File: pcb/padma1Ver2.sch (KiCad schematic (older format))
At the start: 15 parts, among them SW1 SPST, U1 NodeMCU_Amica_R2

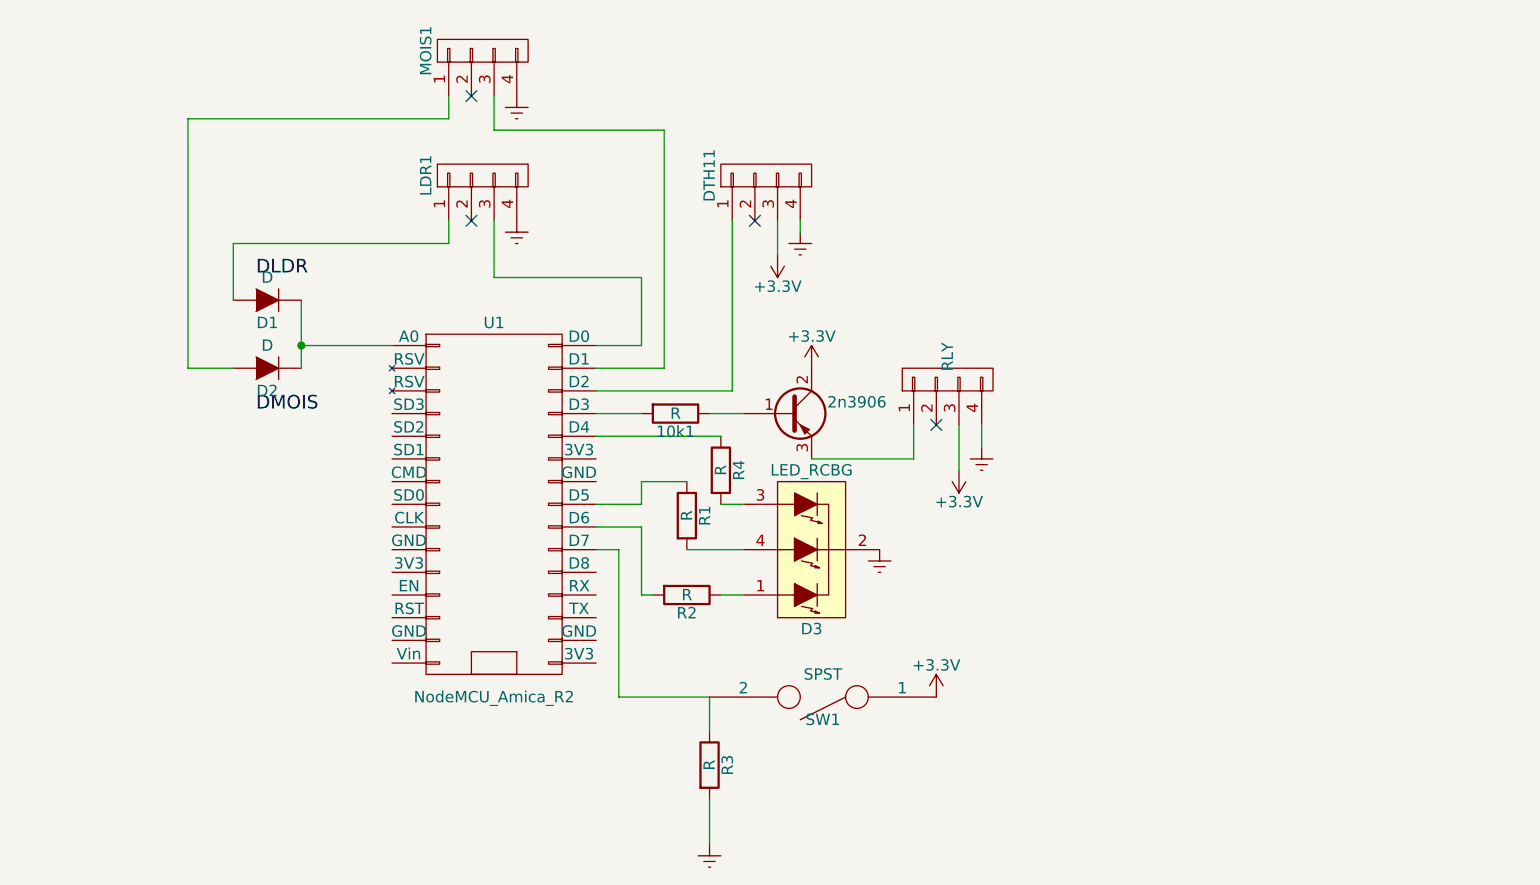
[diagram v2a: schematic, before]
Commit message: with no electrical errors
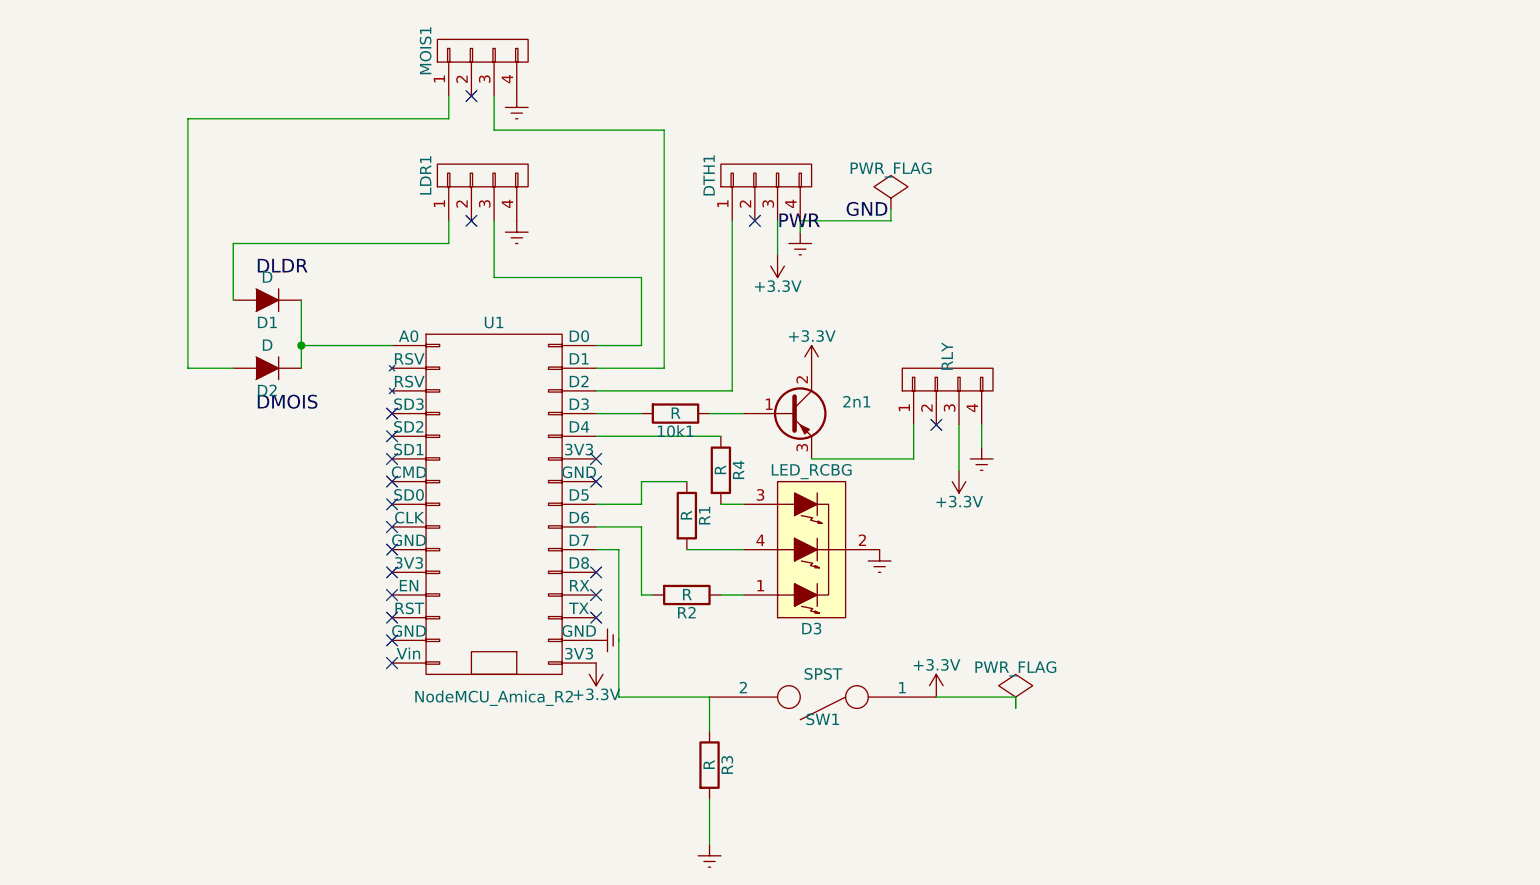
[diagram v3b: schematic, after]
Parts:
- renumbered 2n3906 to 2n1, DTH11 to DTH1
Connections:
- net +3V3: now also U1.16 (3V3)
- net Earth: now also U1.17 (GND)
- no-connect marks 4 -> 21
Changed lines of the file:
@@
 $EndDescr
-$Comp
-L NodeMCU_Amica_R2 U1
-U 1 1 582C3605
-P 4650 3500
-F 0 "U1" H 4650 4300 50  0000 C CNN
-F 1 "NodeMCU_Amica_R2" H 4650 2650 50  0000 C CNN
-F 2 "" H 4900 3500 50  0000 C CNN
-F 3 "" H 4900 3500 50  0000 C CNN
-	1    4650 3500
-	1    0    0    -1
-$EndComp
 $Comp
 L R R3
@@
 $EndComp
 $Comp
-L Q_PNP_BCE 2n3906
+L Q_PNP_BCE 2n1
 U 1 1 582C37C4
 P 5950 3100
-F 0 "2n3906" H 6250 3150 50  0000 C CNN
+F 0 "2n1" H 6250 3150 50  0000 C CNN
 F 1 "Q_PNP_BCE" H 6550 3050 50  0001 R CNN
 F 2 "" H 6150 3200 50  0000 C CNN
@@
 $EndComp
 $Comp
-L CONN_01X04 DTH11
+L CONN_01X04 DTH1
 U 1 1 582C4013
 P 5850 2050
-F 0 "DTH11" H 5850 2300 50  0000 C CNN
+F 0 "DTH1" H 5850 2300 50  0000 C CNN
 F 1 "CONN_01X04" V 5950 2050 50  0001 C CNN
 F 2 "" H 5850 2050 50  0000 C CNN
@@
 NoConn ~ 4550 1700
 $Comp
-L Earth #PWR2
+L Earth #PWR01
 U 1 1 582C4AC2
 P 4750 2250
-F 0 "#PWR2" H 4750 2000 50  0001 C CNN
+F 0 "#PWR01" H 4750 2000 50  0001 C CNN
 F 1 "Earth" H 4750 2100 50  0001 C CNN
 F 2 "" H 4750 2250 50  0000 C CNN
@@
 $EndComp
 $Comp
-L +3.3V #PWR6
+L +3.3V #PWR02
 U 1 1 582C5C13
 P 6050 2900
-F 0 "#PWR6" H 6050 2750 50  0001 C CNN
+F 0 "#PWR02" H 6050 2750 50  0001 C CNN
 F 1 "+3.3V" H 6050 3040 50  0000 C CNN
 F 2 "" H 6050 2900 50  0000 C CNN
@@
 $EndComp
 $Comp
-L Earth #PWR1
+L Earth #PWR03
 U 1 1 582C693C
 P 4750 1700
-F 0 "#PWR1" H 4750 1450 50  0001 C CNN
+F 0 "#PWR03" H 4750 1450 50  0001 C CNN
 F 1 "Earth" H 4750 1550 50  0001 C CNN
 F 2 "" H 4750 1700 50  0000 C CNN
@@
 NoConn ~ 5800 2250
 $Comp
-L +3.3V #PWR4
+L +3.3V #PWR04
 U 1 1 582C7499
 P 5900 2400
-F 0 "#PWR4" H 5900 2250 50  0001 C CNN
+F 0 "#PWR04" H 5900 2250 50  0001 C CNN
 F 1 "+3.3V" H 5900 2540 50  0000 C CNN
 F 2 "" H 5900 2400 50  0000 C CNN
@@
 $EndComp
 $Comp
-L Earth #PWR5
+L Earth #PWR05
 U 1 1 582C7550
 P 6000 2300
-F 0 "#PWR5" H 6000 2050 50  0001 C CNN
+F 0 "#PWR05" H 6000 2050 50  0001 C CNN
 F 1 "Earth" H 6000 2150 50  0001 C CNN
 F 2 "" H 6000 2300 50  0000 C CNN
@@
 NoConn ~ 6600 3150
 $Comp
-L +3.3V #PWR9
+L +3.3V #PWR06
 U 1 1 582C78ED
 P 6700 3350
-F 0 "#PWR9" H 6700 3200 50  0001 C CNN
+F 0 "#PWR06" H 6700 3200 50  0001 C CNN
 F 1 "+3.3V" H 6700 3490 50  0000 C CNN
 F 2 "" H 6700 3350 50  0000 C CNN
@@
 $EndComp
 $Comp
-L Earth #PWR10
+L Earth #PWR07
 U 1 1 582C79CF
 P 6800 3250
-F 0 "#PWR10" H 6800 3000 50  0001 C CNN
+F 0 "#PWR07" H 6800 3000 50  0001 C CNN
 F 1 "Earth" H 6800 3100 50  0001 C CNN
 F 2 "" H 6800 3250 50  0000 C CNN
@@
 $EndComp
 $Comp
-L Earth #PWR7
+L Earth #PWR08
 U 1 1 582C8C6A
 P 6350 3700
-F 0 "#PWR7" H 6350 3450 50  0001 C CNN
+F 0 "#PWR08" H 6350 3450 50  0001 C CNN
 F 1 "Earth" H 6350 3550 50  0001 C CNN
 F 2 "" H 6350 3700 50  0000 C CNN
@@
 	1    0    0    -1
 $EndComp
-Wire Wire Line
-	3800 2600 3800 2900
-Wire Wire Line
-	4200 2800 3800 2800
-Connection ~ 3800 2800
-Wire Wire Line
-	3500 2600 3500 2350
-Wire Wire Line
-	3300 2900 3500 2900
-Wire Wire Line
-	3300 1800 3300 2900
-Wire Wire Line
-	3300 1800 4450 1800
-Wire Wire Line
-	4450 1800 4450 1700
-Wire Wire Line
-	3500 2350 4450 2350
-Wire Wire Line
-	4450 2350 4450 2250
-Wire Wire Line
-	5100 2800 5300 2800
-Wire Wire Line
-	5300 2800 5300 2500
-Wire Wire Line
-	5300 2500 4650 2500
-Wire Wire Line
-	4650 2500 4650 2250
-Wire Wire Line
-	5100 2900 5400 2900
-Wire Wire Line
-	5100 3100 5300 3100
-Wire Wire Line
-	5600 3100 5750 3100
-Wire Wire Line
-	4650 1700 4650 1850
-Wire Wire Line
-	4650 1850 5400 1850
-Wire Wire Line
-	5400 1850 5400 2900
-Wire Wire Line
-	5100 3000 5700 3000
-Wire Wire Line
-	5700 3000 5700 2250
-Wire Wire Line
-	5900 2250 5900 2400
-Wire Wire Line
-	6000 2250 6000 2300
-Wire Wire Line
-	6050 3300 6500 3300
-Wire Wire Line
-	6500 3300 6500 3150
-Wire Wire Line
-	6700 3350 6700 3150
-Wire Wire Line
-	6800 3250 6800 3150
-Wire Wire Line
-	5100 3200 5650 3200
-Wire Wire Line
-	5650 3500 5750 3500
-Wire Wire Line
-	5100 3500 5300 3500
-Wire Wire Line
-	5300 3500 5300 3400
-Wire Wire Line
-	5300 3400 5500 3400
-Wire Wire Line
-	5500 3700 5750 3700
-Wire Wire Line
-	5650 3900 5750 3900
-Wire Wire Line
-	5100 3600 5300 3600
-Wire Wire Line
-	5300 3600 5300 3900
-Wire Wire Line
-	5300 3900 5350 3900
-Wire Wire Line
-	5600 4500 5600 4350
-Wire Wire Line
-	5100 3700 5200 3700
-Wire Wire Line
-	5200 3700 5200 4350
-Wire Wire Line
-	5200 4350 5600 4350
-$Comp
-L Earth #PWR3
+$Comp
+L Earth #PWR09
 U 1 1 582C92CF
 P 5600 5000
-F 0 "#PWR3" H 5600 4750 50  0001 C CNN
+F 0 "#PWR09" H 5600 4750 50  0001 C CNN
 F 1 "Earth" H 5600 4850 50  0001 C CNN
 F 2 "" H 5600 5000 50  0000 C CNN
@@
 	1    0    0    -1
 $EndComp
-Wire Wire Line
-	5600 5000 5600 4800
-$Comp
-L +3.3V #PWR8
+$Comp
+L +3.3V #PWR010
 U 1 1 582C937E
 P 6600 4350
-F 0 "#PWR8" H 6600 4200 50  0001 C CNN
+F 0 "#PWR010" H 6600 4200 50  0001 C CNN
 F 1 "+3.3V" H 6600 4490 50  0000 C CNN
 F 2 "" H 6600 4350 50  0000 C CNN
@@
 	1    0    0    -1
 $EndComp
+$Comp
+L PWR_FLAG #FLG011
+U 1 1 582CAB1D
+P 6400 2200
+F 0 "#FLG011" H 6400 2295 50  0001 C CNN
+F 1 "PWR_FLAG" H 6400 2380 50  0000 C CNN
+F 2 "" H 6400 2200 50  0000 C CNN
+F 3 "" H 6400 2200 50  0000 C CNN
+	1    6400 2200
+	1    0    0    -1
+$EndComp
+$Comp
+L PWR_FLAG #FLG012
+U 1 1 582CAB85
+P 6950 4400
+F 0 "#FLG012" H 6950 4495 50  0001 C CNN
+F 1 "PWR_FLAG" H 6950 4580 50  0000 C CNN
+F 2 "" H 6950 4400 50  0000 C CNN
+F 3 "" H 6950 4400 50  0000 C CNN
+	1    6950 4400
+	1    0    0    -1
+$EndComp
+Wire Wire Line
+	3800 2600 3800 2900
+Wire Wire Line
+	4200 2800 3800 2800
+Connection ~ 3800 2800
+Wire Wire Line
+	3500 2600 3500 2350
+Wire Wire Line
+	3300 2900 3500 2900
+Wire Wire Line
+	3300 1800 3300 2900
+Wire Wire Line
+	3300 1800 4450 1800
+Wire Wire Line
+	4450 1800 4450 1700
+Wire Wire Line
+	3500 2350 4450 2350
+Wire Wire Line
+	4450 2350 4450 2250
+Wire Wire Line
+	5100 2800 5300 2800
+Wire Wire Line
+	5300 2800 5300 2500
+Wire Wire Line
+	5300 2500 4650 2500
+Wire Wire Line
+	4650 2500 4650 2250
+Wire Wire Line
+	5100 2900 5400 2900
+Wire Wire Line
+	5100 3100 5300 3100
+Wire Wire Line
+	5600 3100 5750 3100
+Wire Wire Line
+	4650 1700 4650 1850
+Wire Wire Line
+	4650 1850 5400 1850
+Wire Wire Line
+	5400 1850 5400 2900
+Wire Wire Line
+	5100 3000 5700 3000
+Wire Wire Line
+	5700 3000 5700 2250
+Wire Wire Line
+	5900 2250 5900 2400
+Wire Wire Line
+	6000 2250 6000 2300
+Wire Wire Line
+	6050 3300 6500 3300
+Wire Wire Line
+	6500 3300 6500 3150
+Wire Wire Line
+	6700 3350 6700 3150
+Wire Wire Line
+	6800 3250 6800 3150
+Wire Wire Line
+	5100 3200 5650 3200
+Wire Wire Line
+	5650 3500 5750 3500
+Wire Wire Line
+	5100 3500 5300 3500
+Wire Wire Line
+	5300 3500 5300 3400
+Wire Wire Line
+	5300 3400 5500 3400
+Wire Wire Line
+	5500 3700 5750 3700
+Wire Wire Line
+	5650 3900 5750 3900
+Wire Wire Line
+	5100 3600 5300 3600
+Wire Wire Line
+	5300 3600 5300 3900
+Wire Wire Line
+	5300 3900 5350 3900
+Wire Wire Line
+	5600 4500 5600 4350
+Wire Wire Line
+	5100 3700 5200 3700
+Wire Wire Line
+	5200 3700 5200 4350
+Wire Wire Line
+	5200 4350 5600 4350
+Wire Wire Line
+	5600 5000 5600 4800
+Wire Wire Line
+	6400 2200 6400 2250
+Wire Wire Line
+	6400 2250 6000 2250
+Wire Wire Line
+	6600 4350 6950 4350
+Wire Wire Line
+	6950 4350 6950 4400
+Text Label 6200 2250 0    60   ~ 0
+GND
+Text Label 5900 2300 0    60   ~ 0
+PWR
+NoConn ~ 4200 3100
+NoConn ~ 4200 3200
+NoConn ~ 4200 3300
+NoConn ~ 4200 3400
+NoConn ~ 4200 3500
+NoConn ~ 4200 3600
+NoConn ~ 4200 3700
+NoConn ~ 4200 3800
+NoConn ~ 4200 4200
+NoConn ~ 5100 4000
+NoConn ~ 5100 3400
+NoConn ~ 4200 4100
+NoConn ~ 4200 3900
+$Comp
+L NodeMCU_Amica_R2 U1
+U 1 1 582C3605
+P 4650 3500
+F 0 "U1" H 4650 4300 50  0000 C CNN
+F 1 "NodeMCU_Amica_R2" H 4650 2650 50  0000 C CNN
+F 2 "" H 4900 3500 50  0000 C CNN
+F 3 "" H 4900 3500 50  0000 C CNN
+	1    4650 3500
+	1    0    0    -1
+$EndComp
+$Comp
+L +3.3V #PWR013
+U 1 1 582CBB12
+P 5100 4200
+F 0 "#PWR013" H 5100 4050 50  0001 C CNN
+F 1 "+3.3V" H 5100 4340 50  0000 C CNN
+F 2 "" H 5100 4200 50  0000 C CNN
+F 3 "" H 5100 4200 50  0000 C CNN
+	1    5100 4200
+	-1   0    0    1
+$EndComp
+$Comp
+L Earth #PWR014
+U 1 1 582CBC4D
+P 5100 4100
+F 0 "#PWR014" H 5100 3850 50  0001 C CNN
+F 1 "Earth" H 5100 3950 50  0001 C CNN
+F 2 "" H 5100 4100 50  0000 C CNN
+F 3 "" H 5100 4100 50  0000 C CNN
+	1    5100 4100
+	0    -1   -1   0
+$EndComp
+NoConn ~ 5100 3900
+NoConn ~ 5100 3800
+NoConn ~ 5100 3300
+NoConn ~ 4200 4000
 $EndSCHEMATC

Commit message: added WebApp files by Prof A Mohan
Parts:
- renumbered 2n1 to 2n3906
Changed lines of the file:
@@
 F 0 "R3" V 5680 4650 50  0000 C CNN
 F 1 "R" V 5600 4650 50  0000 C CNN
-F 2 "" V 5530 4650 50  0000 C CNN
+F 2 "" V 5530 4650 50  0001 C CNN
 F 3 "" H 5600 4650 50  0000 C CNN
 	1    5600 4650
@@
 F 0 "10k1" V 5530 3100 50  0000 C CNN
 F 1 "R" V 5450 3100 50  0000 C CNN
-F 2 "" V 5380 3100 50  0000 C CNN
+F 2 "" V 5380 3100 50  0001 C CNN
 F 3 "" H 5450 3100 50  0000 C CNN
 	1    5450 3100
@@
 F 0 "D2" H 3650 3000 50  0000 C CNN
 F 1 "D" H 3650 2800 50  0000 C CNN
-F 2 "" H 3650 2900 50  0000 C CNN
+F 2 "" H 3650 2900 50  0001 C CNN
 F 3 "" H 3650 2900 50  0000 C CNN
 	1    3650 2900
@@
 $EndComp
 $Comp
-L Q_PNP_BCE 2n1
+L Q_PNP_BCE 2n3906
 U 1 1 582C37C4
 P 5950 3100
-F 0 "2n1" H 6250 3150 50  0000 C CNN
+F 0 "2n3906" H 6250 3150 50  0000 C CNN
 F 1 "Q_PNP_BCE" H 6550 3050 50  0001 R CNN
-F 2 "" H 6150 3200 50  0000 C CNN
+F 2 "" H 6150 3200 50  0001 C CNN
 F 3 "" H 5950 3100 50  0000 C CNN
 	1    5950 3100
@@
 F 0 "SW1" H 6100 4450 50  0000 C CNN
 F 1 "SPST" H 6100 4250 50  0000 C CNN
-F 2 "" H 6100 4350 50  0000 C CNN
+F 2 "" H 6100 4350 50  0001 C CNN
 F 3 "" H 6100 4350 50  0000 C CNN
 	1    6100 4350
@@
 F 0 "D1" H 3650 2700 50  0000 C CNN
 F 1 "D" H 3650 2500 50  0000 C CNN
-F 2 "" H 3650 2600 50  0000 C CNN
+F 2 "" H 3650 2600 50  0001 C CNN
 F 3 "" H 3650 2600 50  0000 C CNN
 	1    3650 2600
@@
 F 0 "LDR1" H 4600 2300 50  0000 C CNN
 F 1 "CONN_01X04" V 4700 2050 50  0001 C CNN
-F 2 "" H 4600 2050 50  0000 C CNN
+F 2 "" H 4600 2050 50  0001 C CNN
 F 3 "" H 4600 2050 50  0000 C CNN
 	1    4600 2050
@@
 F 0 "MOIS1" H 4600 1750 50  0000 C CNN
 F 1 "CONN_01X04" V 4700 1500 50  0001 C CNN
-F 2 "" H 4600 1500 50  0000 C CNN
+F 2 "" H 4600 1500 50  0001 C CNN
 F 3 "" H 4600 1500 50  0000 C CNN
 	1    4600 1500
@@
 F 0 "DTH1" H 5850 2300 50  0000 C CNN
 F 1 "CONN_01X04" V 5950 2050 50  0001 C CNN
-F 2 "" H 5850 2050 50  0000 C CNN
+F 2 "" H 5850 2050 50  0001 C CNN
 F 3 "" H 5850 2050 50  0000 C CNN
 	1    5850 2050
@@
 F 0 "Grovr1" H 6650 3200 50  0001 C CNN
 F 1 "RLY" H 6750 2950 50  0000 C CNN
-F 2 "" H 6650 2950 50  0000 C CNN
+F 2 "" H 6650 2950 50  0001 C CNN
 F 3 "" H 6650 2950 50  0000 C CNN
 	1    6650 2950
@@
 F 0 "D3" H 6050 4050 50  0000 C CNN
 F 1 "LED_RCBG" H 6050 3350 50  0000 C CNN
-F 2 "" H 6050 3650 50  0000 C CNN
+F 2 "" H 6050 3650 50  0001 C CNN
 F 3 "" H 6050 3650 50  0000 C CNN
 	1    6050 3700
@@
 F 0 "R4" V 5730 3350 50  0000 C CNN
 F 1 "R" V 5650 3350 50  0000 C CNN
-F 2 "" V 5580 3350 50  0000 C CNN
+F 2 "" V 5580 3350 50  0001 C CNN
 F 3 "" H 5650 3350 50  0000 C CNN
 	1    5650 3350
@@
 F 0 "R1" V 5580 3550 50  0000 C CNN
 F 1 "R" V 5500 3550 50  0000 C CNN
-F 2 "" V 5430 3550 50  0000 C CNN
+F 2 "" V 5430 3550 50  0001 C CNN
 F 3 "" H 5500 3550 50  0000 C CNN
 	1    5500 3550
@@
 F 0 "R2" V 5580 3900 50  0000 C CNN
 F 1 "R" V 5500 3900 50  0000 C CNN
-F 2 "" V 5430 3900 50  0000 C CNN
+F 2 "" V 5430 3900 50  0001 C CNN
 F 3 "" H 5500 3900 50  0000 C CNN
 	1    5500 3900
@@
 F 0 "U1" H 4650 4300 50  0000 C CNN
 F 1 "NodeMCU_Amica_R2" H 4650 2650 50  0000 C CNN
-F 2 "" H 4900 3500 50  0000 C CNN
+F 2 "" H 4900 3500 50  0001 C CNN
 F 3 "" H 4900 3500 50  0000 C CNN
 	1    4650 3500

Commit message: added nodemcu footprint
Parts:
- SW1: footprint (none) -> Buttons_Switches_SMD:SW_SPST_EVPBF
- nodemcu1: renamed from U1; value NodeMCU_Amica_R2 -> nodemcu
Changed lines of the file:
@@
 LIBS:nodemcu
 LIBS:w_relay
+LIBS:padma1Ver2-cache
 EELAYER 25 0
 EELAYER END
@@
 F 0 "SW1" H 6100 4450 50  0000 C CNN
 F 1 "SPST" H 6100 4250 50  0000 C CNN
-F 2 "" H 6100 4350 50  0001 C CNN
+F 2 "Buttons_Switches_SMD:SW_SPST_EVPBF" H 6100 4350 50  0001 C CNN
 F 3 "" H 6100 4350 50  0000 C CNN
 	1    6100 4350
@@
 NoConn ~ 4550 1700
 $Comp
-L Earth #PWR01
+L Earth #PWR2
 U 1 1 582C4AC2
 P 4750 2250
-F 0 "#PWR01" H 4750 2000 50  0001 C CNN
+F 0 "#PWR2" H 4750 2000 50  0001 C CNN
 F 1 "Earth" H 4750 2100 50  0001 C CNN
 F 2 "" H 4750 2250 50  0000 C CNN
@@
 $EndComp
 $Comp
-L +3.3V #PWR02
+L +3.3V #PWR8
 U 1 1 582C5C13
 P 6050 2900
-F 0 "#PWR02" H 6050 2750 50  0001 C CNN
+F 0 "#PWR8" H 6050 2750 50  0001 C CNN
 F 1 "+3.3V" H 6050 3040 50  0000 C CNN
 F 2 "" H 6050 2900 50  0000 C CNN
@@
 $EndComp
 $Comp
-L Earth #PWR03
+L Earth #PWR1
 U 1 1 582C693C
 P 4750 1700
-F 0 "#PWR03" H 4750 1450 50  0001 C CNN
+F 0 "#PWR1" H 4750 1450 50  0001 C CNN
 F 1 "Earth" H 4750 1550 50  0001 C CNN
 F 2 "" H 4750 1700 50  0000 C CNN
@@
 NoConn ~ 5800 2250
 $Comp
-L +3.3V #PWR04
+L +3.3V #PWR6
 U 1 1 582C7499
 P 5900 2400
-F 0 "#PWR04" H 5900 2250 50  0001 C CNN
+F 0 "#PWR6" H 5900 2250 50  0001 C CNN
 F 1 "+3.3V" H 5900 2540 50  0000 C CNN
 F 2 "" H 5900 2400 50  0000 C CNN
@@
 $EndComp
 $Comp
-L Earth #PWR05
+L Earth #PWR7
 U 1 1 582C7550
 P 6000 2300
-F 0 "#PWR05" H 6000 2050 50  0001 C CNN
+F 0 "#PWR7" H 6000 2050 50  0001 C CNN
 F 1 "Earth" H 6000 2150 50  0001 C CNN
 F 2 "" H 6000 2300 50  0000 C CNN
@@
 NoConn ~ 6600 3150
 $Comp
-L +3.3V #PWR06
+L +3.3V #PWR11
 U 1 1 582C78ED
 P 6700 3350
-F 0 "#PWR06" H 6700 3200 50  0001 C CNN
+F 0 "#PWR11" H 6700 3200 50  0001 C CNN
 F 1 "+3.3V" H 6700 3490 50  0000 C CNN
 F 2 "" H 6700 3350 50  0000 C CNN
@@
 $EndComp
 $Comp
-L Earth #PWR07
+L Earth #PWR12
 U 1 1 582C79CF
 P 6800 3250
-F 0 "#PWR07" H 6800 3000 50  0001 C CNN
+F 0 "#PWR12" H 6800 3000 50  0001 C CNN
 F 1 "Earth" H 6800 3100 50  0001 C CNN
 F 2 "" H 6800 3250 50  0000 C CNN
@@
 $EndComp
 $Comp
-L Earth #PWR08
+L Earth #PWR9
 U 1 1 582C8C6A
 P 6350 3700
-F 0 "#PWR08" H 6350 3450 50  0001 C CNN
+F 0 "#PWR9" H 6350 3450 50  0001 C CNN
 F 1 "Earth" H 6350 3550 50  0001 C CNN
 F 2 "" H 6350 3700 50  0000 C CNN
@@
 $EndComp
 $Comp
-L Earth #PWR09
+L Earth #PWR5
 U 1 1 582C92CF
 P 5600 5000
-F 0 "#PWR09" H 5600 4750 50  0001 C CNN
+F 0 "#PWR5" H 5600 4750 50  0001 C CNN
 F 1 "Earth" H 5600 4850 50  0001 C CNN
 F 2 "" H 5600 5000 50  0000 C CNN
@@
 $EndComp
 $Comp
-L +3.3V #PWR010
+L +3.3V #PWR10
 U 1 1 582C937E
 P 6600 4350
-F 0 "#PWR010" H 6600 4200 50  0001 C CNN
+F 0 "#PWR10" H 6600 4200 50  0001 C CNN
 F 1 "+3.3V" H 6600 4490 50  0000 C CNN
 F 2 "" H 6600 4350 50  0000 C CNN
@@
 $EndComp
 $Comp
-L PWR_FLAG #FLG011
+L PWR_FLAG #FLG1
 U 1 1 582CAB1D
 P 6400 2200
-F 0 "#FLG011" H 6400 2295 50  0001 C CNN
+F 0 "#FLG1" H 6400 2295 50  0001 C CNN
 F 1 "PWR_FLAG" H 6400 2380 50  0000 C CNN
 F 2 "" H 6400 2200 50  0000 C CNN
@@
 $EndComp
 $Comp
-L PWR_FLAG #FLG012
+L PWR_FLAG #FLG2
 U 1 1 582CAB85
 P 6950 4400
-F 0 "#FLG012" H 6950 4495 50  0001 C CNN
+F 0 "#FLG2" H 6950 4495 50  0001 C CNN
 F 1 "PWR_FLAG" H 6950 4580 50  0000 C CNN
 F 2 "" H 6950 4400 50  0000 C CNN
@@
 NoConn ~ 4200 3900
 $Comp
-L NodeMCU_Amica_R2 U1
+L NodeMCU_Amica_R2 nodemcu1
 U 1 1 582C3605
 P 4650 3500
-F 0 "U1" H 4650 4300 50  0000 C CNN
-F 1 "NodeMCU_Amica_R2" H 4650 2650 50  0000 C CNN
+F 0 "nodemcu1" H 4650 4300 50  0000 C CNN
+F 1 "nodemcu" H 4650 2650 50  0000 C CNN
 F 2 "" H 4900 3500 50  0001 C CNN
 F 3 "" H 4900 3500 50  0000 C CNN
@@
 $EndComp
 $Comp
-L +3.3V #PWR013
+L +3.3V #PWR4
 U 1 1 582CBB12
 P 5100 4200
-F 0 "#PWR013" H 5100 4050 50  0001 C CNN
+F 0 "#PWR4" H 5100 4050 50  0001 C CNN
 F 1 "+3.3V" H 5100 4340 50  0000 C CNN
 F 2 "" H 5100 4200 50  0000 C CNN
@@
 $EndComp
 $Comp
-L Earth #PWR014
+L Earth #PWR3
 U 1 1 582CBC4D
 P 5100 4100
-F 0 "#PWR014" H 5100 3850 50  0001 C CNN
+F 0 "#PWR3" H 5100 3850 50  0001 C CNN
 F 1 "Earth" H 5100 3950 50  0001 C CNN
 F 2 "" H 5100 4100 50  0000 C CNN
